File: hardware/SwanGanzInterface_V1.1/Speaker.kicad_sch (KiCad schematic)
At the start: 12 parts, among them J12 SPKM.28.8.A, J13 Conn_01x06_Pin, U12 MCP34119P, U13 AdaFruit_1590

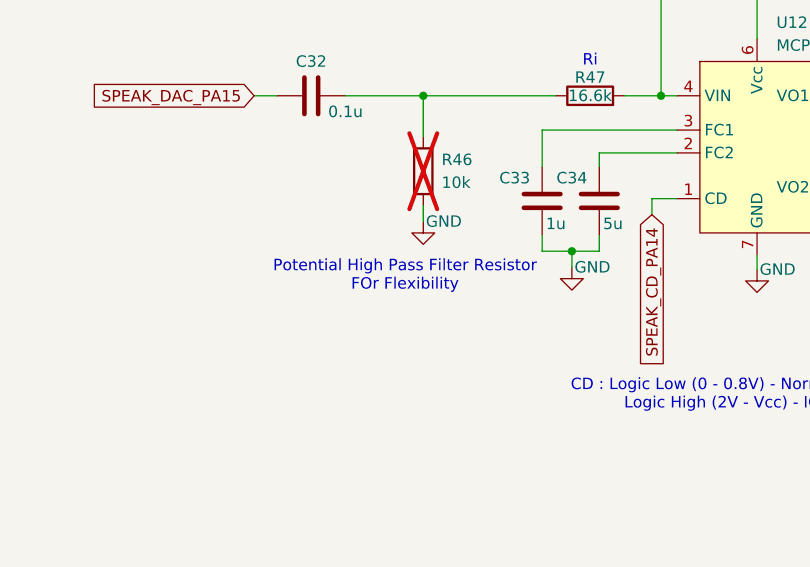
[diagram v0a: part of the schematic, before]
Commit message: Filter paramaters and assigned footprints
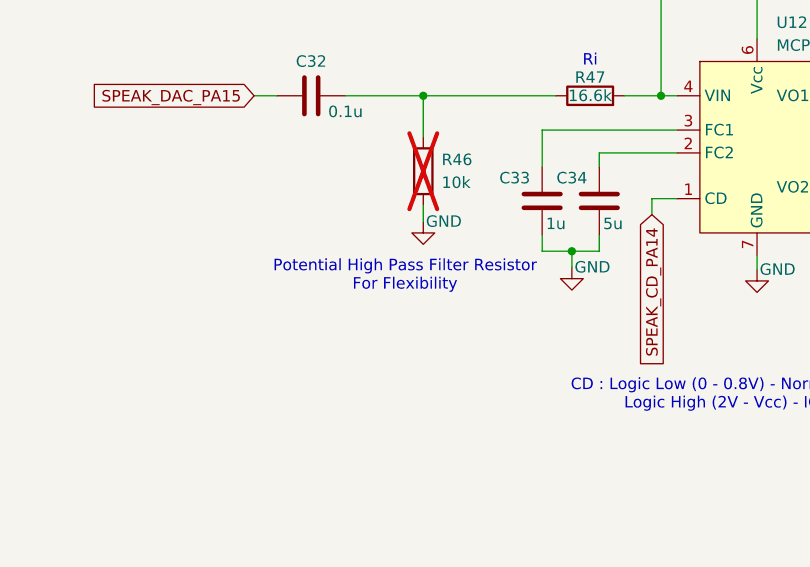
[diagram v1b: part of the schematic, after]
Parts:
- C32, C33, C36: footprint (none) -> Capacitor_SMD:C_0603_1608Metric
- C34: footprint (none) -> Capacitor_SMD:C_1206_3216Metric
- J13: footprint (none) -> Connector_PinHeader_2.54mm:PinHeader_1x06_P2.54mm_Vertical
- R46, R47, R48: footprint (none) -> Resistor_SMD:R_0603_1608Metric
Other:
- note added: "Potential High Pass Filter Resistor For Flexibility"
- note removed: "Potential High Pass Filter Resistor FOr Flexibility"
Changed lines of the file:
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@@
 		)
 	)
-	(text "Potential High Pass Filter Resistor\nFOr Flexibility"
+	(text "Potential High Pass Filter Resistor\nFor Flexibility"
 		(exclude_from_sim no)
 		(at 109.22 71.12 0)
@@
 			)
 		)
-		(property "Footprint" ""
+		(property "Footprint" "Connector_PinHeader_2.54mm:PinHeader_1x06_P2.54mm_Vertical"
 			(at 151.384 164.592 0)
 			(effects
@@
 			)
 		)
-		(property "Footprint" ""
+		(property "Footprint" "Resistor_SMD:R_0603_1608Metric"
 			(at 129.794 52.832 90)
 			(effects
@@
 			)
 		)
-		(property "Footprint" ""
+		(property "Footprint" "Resistor_SMD:R_0603_1608Metric"
 			(at 109.474 59.436 90)
 			(effects
@@
 			)
 		)
-		(property "Footprint" ""
+		(property "Footprint" "Capacitor_SMD:C_1206_3216Metric"
 			(at 129.8448 58.928 0)
 			(effects
@@
 			)
 		)
-		(property "Footprint" ""
+		(property "Footprint" "Capacitor_SMD:C_0603_1608Metric"
 			(at 160.528 38.4048 0)
 			(effects
@@
 			)
 		)
-		(property "Footprint" ""
+		(property "Footprint" "Capacitor_SMD:C_0603_1608Metric"
 			(at 123.4948 58.928 0)
 			(effects
@@
 			)
 		)
-		(property "Footprint" ""
+		(property "Footprint" "Resistor_SMD:R_0603_1608Metric"
 			(at 156.718 31.242 90)
 			(effects
@@
 			)
 		)
-		(property "Footprint" ""
+		(property "Footprint" "Capacitor_SMD:C_0603_1608Metric"
 			(at 102.616 50.0888 0)
 			(effects

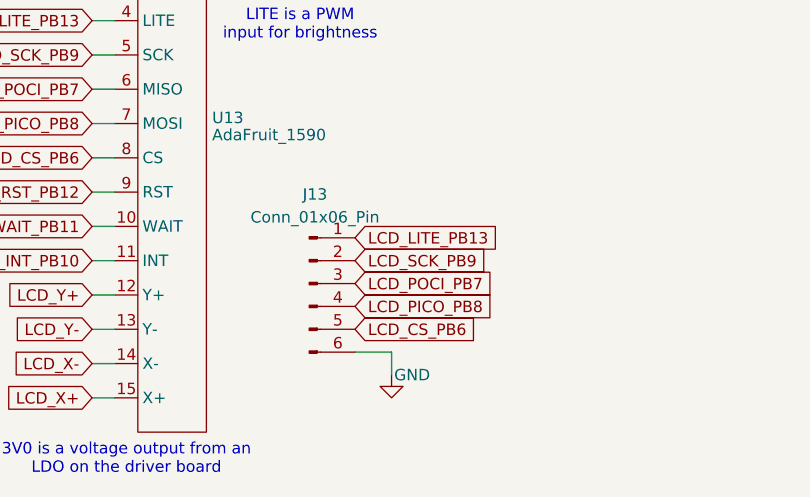
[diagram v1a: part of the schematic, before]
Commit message: Layout work on screen and expanded board size
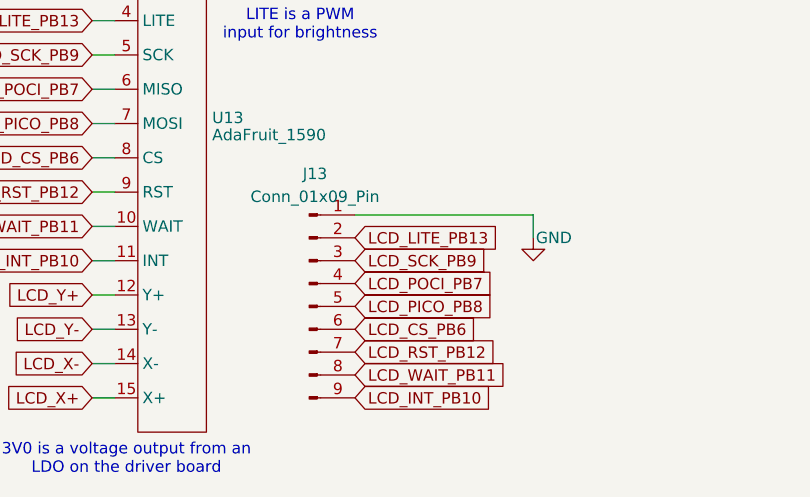
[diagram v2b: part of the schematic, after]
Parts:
- removed J13: Conn_01x06_Pin, Connector_PinHeader_2.54mm:PinHeader_1x06_P2.54mm_Vertical, symbol Connector:Conn_01x06_Pin
- added J13: Conn_01x09_Pin, Connector_PinHeader_2.54mm:PinHeader_1x09_P2.54mm_Vertical, symbol Connector:Conn_01x09_Pin
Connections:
- net GND: now also J13.1 (Pin_1)
- net LCD_CS_PB6: now also J13.6 (Pin_6)
- net LCD_INT_PB10: now also J13.9 (Pin_9)
- net LCD_LITE_PB13: now also J13.2 (Pin_2)
- net LCD_PICO_PB8: now also J13.5 (Pin_5)
- net LCD_POCI_PB7: now also J13.4 (Pin_4)
- net LCD_RST_PB12: now also J13.7 (Pin_7)
- net LCD_SCK_PB9: now also J13.3 (Pin_3)
- net LCD_WAIT_PB11: now also J13.8 (Pin_8)
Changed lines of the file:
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@@
 	(wire
 		(pts
-			(xy 160.528 172.212) (xy 156.464 172.212)
-		)
-		(stroke
-			(width 0)
-			(type default)
-		)
-	)
-	(wire
-		(pts
-			(xy 160.528 174.752) (xy 160.528 172.212)
+			(xy 176.276 159.512) (xy 176.276 156.972)
 		)
 		(stroke
@@
 	(wire
 		(pts
+			(xy 156.464 156.972) (xy 176.276 156.972)
+		)
+		(stroke
+			(width 0)
+			(type default)
+		)
+	)
+	(wire
+		(pts
 			(xy 108.204 127.762) (xy 108.204 136.652)
 		)
@@
 		)
 	)
+	(global_label "LCD_RST_PB12"
+		(shape input)
+		(at 156.464 172.212 0)
+		(fields_autoplaced yes)
+		(effects
+			(font
+				(size 1.27 1.27)
+			)
+			(justify left)
+		)
+		(property "Intersheetrefs" "${INTERSHEET_REFS}"
+			(at 173.3586 172.212 0)
+			(effects
+				(font
+					(size 1.27 1.27)
+				)
+				(justify left)
+				(hide yes)
+			)
+		)
+	)
+	(global_label "LCD_INT_PB10"
+		(shape input)
+		(at 156.464 177.292 0)
+		(fields_autoplaced yes)
+		(effects
+			(font
+				(size 1.27 1.27)
+			)
+			(justify left)
+		)
+		(property "Intersheetrefs" "${INTERSHEET_REFS}"
+			(at 172.8144 177.292 0)
+			(effects
+				(font
+					(size 1.27 1.27)
+				)
+				(justify left)
+				(hide yes)
+			)
+		)
+	)
 	(global_label "LCD_PICO_PB8"
 		(shape input)
@@
 				)
 				(justify right)
+				(hide yes)
+			)
+		)
+	)
+	(global_label "LCD_WAIT_PB11"
+		(shape input)
+		(at 156.464 174.752 0)
+		(fields_autoplaced yes)
+		(effects
+			(font
+				(size 1.27 1.27)
+			)
+			(justify left)
+		)
+		(property "Intersheetrefs" "${INTERSHEET_REFS}"
+			(at 174.0239 174.752 0)
+			(effects
+				(font
+					(size 1.27 1.27)
+				)
+				(justify left)
 				(hide yes)
 			)
@@
 				(path "/4e9a6e30-f660-472b-9696-bea1f34b4545/f7080da7-b463-4c5e-88b4-efa970c84168"
 					(reference "#PWR093")
-					(unit 1)
-				)
-			)
-		)
-	)
-	(symbol
-		(lib_id "Connector:Conn_01x06_Pin")
-		(at 151.384 164.592 0)
-		(unit 1)
-		(exclude_from_sim no)
-		(in_bom yes)
-		(on_board yes)
-		(dnp no)
-		(fields_autoplaced yes)
-		(property "Reference" "J13"
-			(at 152.019 154.686 0)
-			(effects
-				(font
-					(size 1.27 1.27)
-				)
-			)
-		)
-		(property "Value" "Conn_01x06_Pin"
-			(at 152.019 157.226 0)
-			(effects
-				(font
-					(size 1.27 1.27)
-				)
-			)
-		)
-		(property "Footprint" "Connector_PinHeader_2.54mm:PinHeader_1x06_P2.54mm_Vertical"
-			(at 151.384 164.592 0)
-			(effects
-				(font
-					(size 1.27 1.27)
-				)
-				(hide yes)
-			)
-		)
-		(property "Datasheet" "~"
-			(at 151.384 164.592 0)
-			(effects
-				(font
-					(size 1.27 1.27)
-				)
-				(hide yes)
-			)
-		)
-		(property "Description" "Generic connector, single row, 01x06, script generated"
-			(at 151.384 164.592 0)
-			(effects
-				(font
-					(size 1.27 1.27)
-				)
-				(hide yes)
-			)
-		)
-		(pin "4"
-		)
-		(pin "2"
-		)
-		(pin "5"
-		)
-		(pin "3"
-		)
-		(pin "1"
-		)
-		(pin "6"
-		)
-		(instances
-			(project ""
-				(path "/4e9a6e30-f660-472b-9696-bea1f34b4545/f7080da7-b463-4c5e-88b4-efa970c84168"
-					(reference "J13")
 					(unit 1)
 				)
@@
 	)
 	(symbol
+		(lib_id "Connector:Conn_01x09_Pin")
+		(at 151.384 167.132 0)
+		(unit 1)
+		(exclude_from_sim no)
+		(in_bom yes)
+		(on_board yes)
+		(dnp no)
+		(fields_autoplaced yes)
+		(property "Reference" "J13"
+			(at 152.019 152.4 0)
+			(effects
+				(font
+					(size 1.27 1.27)
+				)
+			)
+		)
+		(property "Value" "Conn_01x09_Pin"
+			(at 152.019 154.94 0)
+			(effects
+				(font
+					(size 1.27 1.27)
+				)
+			)
+		)
+		(property "Footprint" "Connector_PinHeader_2.54mm:PinHeader_1x09_P2.54mm_Vertical"
+			(at 151.384 167.132 0)
+			(effects
+				(font
+					(size 1.27 1.27)
+				)
+				(hide yes)
+			)
+		)
+		(property "Datasheet" "~"
+			(at 151.384 167.132 0)
+			(effects
+				(font
+					(size 1.27 1.27)
+				)
+				(hide yes)
+			)
+		)
+		(property "Description" "Generic connector, single row, 01x09, script generated"
+			(at 151.384 167.132 0)
+			(effects
+				(font
+					(size 1.27 1.27)
+				)
+				(hide yes)
+			)
+		)
+		(pin "1"
+		)
+		(pin "8"
+		)
+		(pin "4"
+		)
+		(pin "2"
+		)
+		(pin "3"
+		)
+		(pin "5"
+		)
+		(pin "6"
+		)
+		(pin "7"
+		)
+		(pin "9"
+		)
+		(instances
+			(project ""
+				(path "/4e9a6e30-f660-472b-9696-bea1f34b4545/f7080da7-b463-4c5e-88b4-efa970c84168"
+					(reference "J13")
+					(unit 1)
+				)
+			)
+		)
+	)
+	(symbol
 		(lib_id "power:+3V3")
 		(at 148.336 36.576 0)
@@
 	(symbol
 		(lib_id "power:GND")
-		(at 160.528 174.752 0)
+		(at 176.276 159.512 0)
 		(unit 1)
 		(exclude_from_sim no)
@@
 		(dnp no)
 		(property "Reference" "#PWR098"
-			(at 160.528 181.102 0)
+			(at 176.276 165.862 0)
 			(effects
 				(font
@@
 		)
 		(property "Value" "GND"
-			(at 162.814 174.752 0)
+			(at 178.562 159.512 0)
 			(effects
 				(font
@@
 		)
 		(property "Footprint" ""
-			(at 160.528 174.752 0)
+			(at 176.276 159.512 0)
 			(effects
 				(font
@@
 		)
 		(property "Datasheet" ""
-			(at 160.528 174.752 0)
+			(at 176.276 159.512 0)
 			(effects
 				(font
@@
 		)
 		(property "Description" "Power symbol creates a global label with name \"GND\" , ground"
-			(at 160.528 174.752 0)
-			(effects
-				(font
+			(at 176.276 159.512 0)
+			(effects
+				(font

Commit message: SGI v2 Layout Complete
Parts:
- renumbered C32 to C35, C35 to C36, C33 to C37, C34 to C38, C36 to C39, J12 to J14, R46 to R50, R47 to R51, R48 to R52, U13 to U14, U12 to U15
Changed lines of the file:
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@@
 		(dnp no)
 		(fields_autoplaced yes)
-		(property "Reference" "C35"
+		(property "Reference" "C36"
 			(at 102.616 129.0319 0)
 			(effects
@@
 			(project "SwanGanzInterface_V1.1"
 				(path "/4e9a6e30-f660-472b-9696-bea1f34b4545/f7080da7-b463-4c5e-88b4-efa970c84168"
-					(reference "C35")
+					(reference "C36")
 					(unit 1)
 				)
@@
 		(dnp no)
 		(fields_autoplaced yes)
-		(property "Reference" "#PWR093"
+		(property "Reference" "#PWR098"
 			(at 98.806 122.682 0)
 			(effects
@@
 			(project "SwanGanzInterface_V1.1"
 				(path "/4e9a6e30-f660-472b-9696-bea1f34b4545/f7080da7-b463-4c5e-88b4-efa970c84168"
-					(reference "#PWR093")
+					(reference "#PWR098")
 					(unit 1)
 				)
@@
 		(on_board yes)
 		(dnp no)
-		(property "Reference" "U13"
+		(property "Reference" "U14"
 			(at 140.589 146.177 0)
 			(effects
@@
 			(project "SwanGanzInterface_V1.1"
 				(path "/4e9a6e30-f660-472b-9696-bea1f34b4545/f7080da7-b463-4c5e-88b4-efa970c84168"
-					(reference "U13")
+					(reference "U14")
 					(unit 1)
 				)
@@
 		(on_board yes)
 		(dnp no)
-		(property "Reference" "R47"
+		(property "Reference" "R51"
 			(at 129.794 49.022 90)
 			(effects
@@
 			(project ""
 				(path "/4e9a6e30-f660-472b-9696-bea1f34b4545/f7080da7-b463-4c5e-88b4-efa970c84168"
-					(reference "R47")
+					(reference "R51")
 					(unit 1)
 				)
@@
 		(dnp yes)
 		(fields_autoplaced yes)
-		(property "Reference" "R46"
+		(property "Reference" "R50"
 			(at 113.284 58.1659 0)
 			(effects
@@
 			(project ""
 				(path "/4e9a6e30-f660-472b-9696-bea1f34b4545/f7080da7-b463-4c5e-88b4-efa970c84168"
-					(reference "R46")
+					(reference "R50")
 					(unit 1)
 				)
@@
 		(on_board yes)
 		(dnp no)
-		(property "Reference" "#PWR092"
+		(property "Reference" "#PWR0101"
 			(at 127.762 76.454 0)
 			(effects
@@
 			(project "SwanGanzInterface_V1.1"
 				(path "/4e9a6e30-f660-472b-9696-bea1f34b4545/f7080da7-b463-4c5e-88b4-efa970c84168"
-					(reference "#PWR092")
+					(reference "#PWR0101")
 					(unit 1)
 				)
@@
 		(on_board yes)
 		(dnp no)
-		(property "Reference" "C34"
+		(property "Reference" "C38"
 			(at 127.762 60.198 0)
 			(effects
@@
 			(project "SwanGanzInterface_V1.1"
 				(path "/4e9a6e30-f660-472b-9696-bea1f34b4545/f7080da7-b463-4c5e-88b4-efa970c84168"
-					(reference "C34")
+					(reference "C38")
 					(unit 1)
 				)
@@
 		(on_board yes)
 		(dnp no)
-		(property "Reference" "#PWR095"
+		(property "Reference" "#PWR0102"
 			(at 148.336 40.386 0)
 			(effects
@@
 			(project ""
 				(path "/4e9a6e30-f660-472b-9696-bea1f34b4545/f7080da7-b463-4c5e-88b4-efa970c84168"
-					(reference "#PWR095")
+					(reference "#PWR0102")
 					(unit 1)
 				)
@@
 		(dnp no)
 		(fields_autoplaced yes)
-		(property "Reference" "#PWR094"
+		(property "Reference" "#PWR099"
 			(at 98.806 145.542 0)
 			(effects
@@
 			(project "SwanGanzInterface_V1.1"
 				(path "/4e9a6e30-f660-472b-9696-bea1f34b4545/f7080da7-b463-4c5e-88b4-efa970c84168"
-					(reference "#PWR094")
+					(reference "#PWR099")
 					(unit 1)
 				)
@@
 		(dnp no)
 		(fields_autoplaced yes)
-		(property "Reference" "J12"
+		(property "Reference" "J14"
 			(at 189.738 52.3239 0)
 			(effects
@@
 			(project "SwanGanzInterface_V1.1"
 				(path "/4e9a6e30-f660-472b-9696-bea1f34b4545/f7080da7-b463-4c5e-88b4-efa970c84168"
-					(reference "J12")
+					(reference "J14")
 					(unit 1)
 				)
@@
 		(dnp no)
 		(fields_autoplaced yes)
-		(property "Reference" "U12"
+		(property "Reference" "U15"
 			(at 150.4793 42.926 0)
 			(effects
@@
 			(project ""
 				(path "/4e9a6e30-f660-472b-9696-bea1f34b4545/f7080da7-b463-4c5e-88b4-efa970c84168"
-					(reference "U12")
+					(reference "U15")
 					(unit 1)
 				)
@@
 		(on_board yes)
 		(dnp no)
-		(property "Reference" "C36"
+		(property "Reference" "C39"
 			(at 156.718 35.56 90)
 			(effects
@@
 			(project ""
 				(path "/4e9a6e30-f660-472b-9696-bea1f34b4545/f7080da7-b463-4c5e-88b4-efa970c84168"
-					(reference "C36")
+					(reference "C39")
 					(unit 1)
 				)
@@
 		(on_board yes)
 		(dnp no)
-		(property "Reference" "#PWR091"
+		(property "Reference" "#PWR0100"
 			(at 111.252 71.374 0)
 			(effects
@@
 			(project "SwanGanzInterface_V1.1"
 				(path "/4e9a6e30-f660-472b-9696-bea1f34b4545/f7080da7-b463-4c5e-88b4-efa970c84168"
-					(reference "#PWR091")
+					(reference "#PWR0100")
 					(unit 1)
 				)
@@
 		(on_board yes)
 		(dnp no)
-		(property "Reference" "#PWR096"
+		(property "Reference" "#PWR0103"
 			(at 148.336 76.708 0)
 			(effects
@@
 			(project "SwanGanzInterface_V1.1"
 				(path "/4e9a6e30-f660-472b-9696-bea1f34b4545/f7080da7-b463-4c5e-88b4-efa970c84168"
-					(reference "#PWR096")
+					(reference "#PWR0103")
 					(unit 1)
 				)
@@
 		(on_board yes)
 		(dnp no)
-		(property "Reference" "#PWR098"
+		(property "Reference" "#PWR0105"
 			(at 176.276 165.862 0)
 			(effects
@@
 			(project "SwanGanzInterface_V1.1"
 				(path "/4e9a6e30-f660-472b-9696-bea1f34b4545/f7080da7-b463-4c5e-88b4-efa970c84168"
-					(reference "#PWR098")
+					(reference "#PWR0105")
 					(unit 1)
 				)
@@
 		(on_board yes)
 		(dnp no)
-		(property "Reference" "C33"
+		(property "Reference" "C37"
 			(at 121.412 60.198 0)
 			(effects
@@
 			(project "SwanGanzInterface_V1.1"
 				(path "/4e9a6e30-f660-472b-9696-bea1f34b4545/f7080da7-b463-4c5e-88b4-efa970c84168"
-					(reference "C33")
+					(reference "C37")
 					(unit 1)
 				)
@@
 		(on_board yes)
 		(dnp no)
-		(property "Reference" "#PWR097"
+		(property "Reference" "#PWR0104"
 			(at 164.846 49.276 0)
 			(effects
@@
 			(project ""
 				(path "/4e9a6e30-f660-472b-9696-bea1f34b4545/f7080da7-b463-4c5e-88b4-efa970c84168"
-					(reference "#PWR097")
+					(reference "#PWR0104")
 					(unit 1)
 				)
@@
 		(on_board yes)
 		(dnp no)
-		(property "Reference" "R48"
+		(property "Reference" "R52"
 			(at 156.718 27.432 90)
 			(effects
@@
 			(project "SwanGanzInterface_V1.1"
 				(path "/4e9a6e30-f660-472b-9696-bea1f34b4545/f7080da7-b463-4c5e-88b4-efa970c84168"
-					(reference "R48")
+					(reference "R52")
 					(unit 1)
 				)
@@
 		(on_board yes)
 		(dnp no)
-		(property "Reference" "C32"
+		(property "Reference" "C35"
 			(at 98.806 47.244 90)
 			(effects
@@
 			(project "SwanGanzInterface_V1.1"
 				(path "/4e9a6e30-f660-472b-9696-bea1f34b4545/f7080da7-b463-4c5e-88b4-efa970c84168"
-					(reference "C32")
-					(unit 1)
-				)
+					(reference "C35")
+					(unit 1)
+				)
